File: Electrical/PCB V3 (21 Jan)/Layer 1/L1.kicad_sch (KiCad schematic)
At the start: 219 parts, among them J1 Conn_01x04, J2 Conn_01x02, Q1 NMOS, U1 LM2587S-ADJ, U2 CD74HC4067SM, U3 CD74HC4067SM, U4 XT30UPB-M, U5 113991054

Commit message: added some stuff to parts list, fixed l1 schematics to fit parts in lab abit more, pending change of activaition circuit
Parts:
- removed L1, L10, L11, L12, L13, L14, L15, L16, L17, L18, L19, L2, L20, L21, L22, L23, L24, L25, L26, L27, L28, L29, L3, L30, L31, L32, L4, L5, L6, L7, L8, L9: 10µH, Inductor_SMD:L_0805_2012Metric, symbol pspice:INDUCTOR
- added Q3: NMOS, Package_TO_SOT_THT:TO-220-3_Vertical, symbol Simulation_SPICE:NMOS
- R35: value 36.9K -> 36.9K/56k
- R36: value 2K -> 2K/2.94k
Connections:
- net GND: now also Q3.3 (S)
- net Solenoid Activation: now also Q3.2 (G); no longer Q1.2 (G)
- net at LED6.2 (A): now also R6.2
- net at LED32.2 (A): now also R32.2
- net at LED5.2 (A): now also R5.2
- net at LED18.2 (A): now also R18.2
- net at LED4.2 (A): now also R4.2
- net at LED8.2 (A): now also R8.2
- net at R9.2: now also LED9.2 (A)
- net at LED30.2 (A): now also R30.2
- net at LED31.2 (A): now also R31.2
- net at R28.2: now also LED28.2 (A)
- net at R29.2: now also LED29.2 (A)
- net at LED26.2 (A): now also R26.2
- net at LED17.2 (A): now also R17.2
- net at LED19.2 (A): now also R19.2
- net at R21.2: now also LED21.2 (A)
- net at LED7.2 (A): now also R7.2
- net at LED10.2 (A): now also R10.2
- net at LED14.2 (A): now also R14.2
- net at LED3.2 (A): now also R3.2
- net at LED25.2 (A): now also R25.2
- net at LED2.2 (A): now also R2.2
- net at LED16.2 (A): now also R16.2
- net at LED20.2 (A): now also R20.2
- net at LED1.2 (A): now also R1.2
- net at LED24.2 (A): now also R24.2
- net at LED27.2 (A): now also R27.2
- net at R13.2: now also LED13.2 (A)
- net at LED12.2 (A): now also R12.2
- net at R15.2: now also LED15.2 (A)
- net at LED11.2 (A): now also R11.2
- net at LED23.2 (A): now also R23.2
- net at R22.2: now also LED22.2 (A)
- new net: Q1.2 (G), Q3.1 (D)
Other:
- moved on the sheet: D2, LED1, LED10, LED11, LED12, LED13, LED14, LED15, LED16, LED17, LED18, LED19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

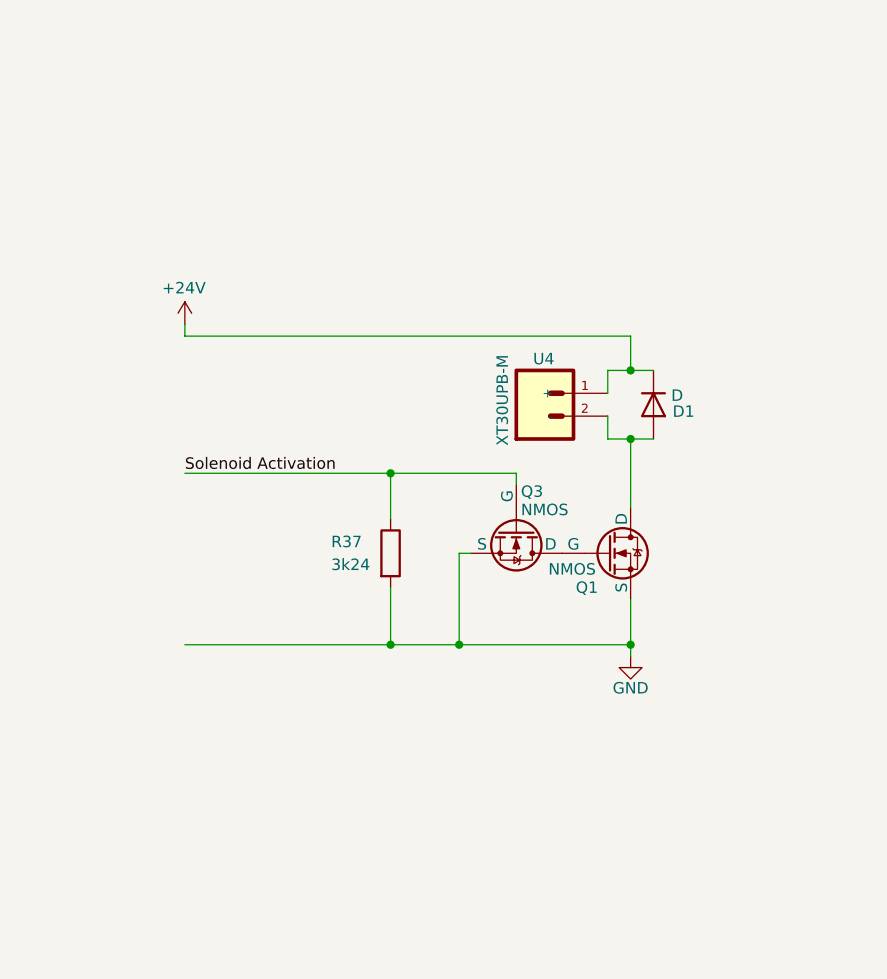
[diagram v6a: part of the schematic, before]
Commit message: fixed l1 solenoid activation circuit
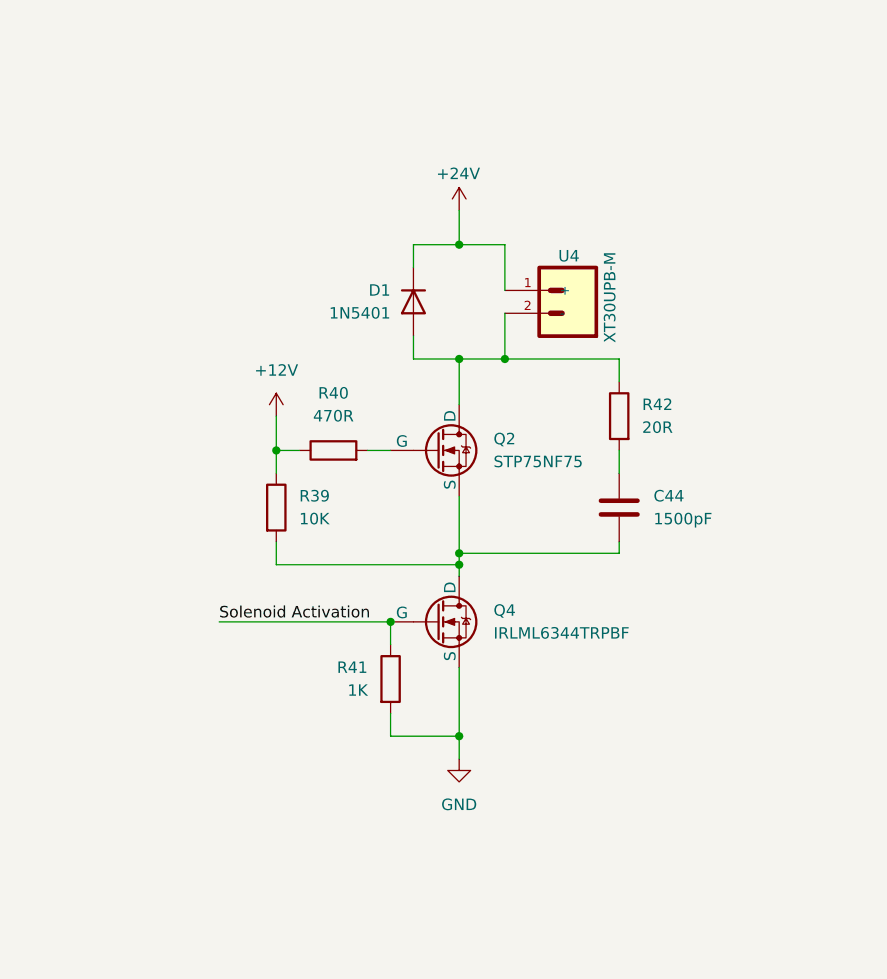
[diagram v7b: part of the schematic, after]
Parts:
- removed D1: D, Diode_THT:D_DO-201AD_P15.24mm_Horizontal, symbol Device:D
- removed Q1, Q3: NMOS, Package_TO_SOT_THT:TO-220-3_Vertical, symbol Simulation_SPICE:NMOS
- removed R37: 3k24, Capacitor_SMD:C_0603_1608Metric, symbol Device:R
- added C44: 1500pF, Capacitor_SMD:C_0603_1608Metric, symbol Device:C
- added D1: 1N5401, Diode_THT:D_DO-201AD_P15.24mm_Horizontal, symbol Diode:1N5401
- added Q2: STP75NF75, stolen_activation_moosfits:TO-220-3_Vertical, symbol vincent:IPD050N10N5ATMA1
- added Q4: IRLML6344TRPBF, stolen_activation_moosfits:SOT95P237X112-3N, symbol vincent:IRLML6344TRPBF
- added R39: 10K, Resistor_SMD:R_0603_1608Metric, symbol Device:R
- added R40: 470R, Resistor_SMD:R_0603_1608Metric, symbol Device:R
- added R41: 1K, Resistor_SMD:R_0603_1608Metric, symbol Device:R
- added R42: 20R, Resistor_SMD:R_0603_1608Metric, symbol Device:R
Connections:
- net +12V: now also R39.1, R40.1
- net +24V: now also D1.1 (K)
- net GND: now also Q4.2 (S), R41.2
- net Solenoid Activation: now also Q4.1 (G), R41.1
- net at U4.2 (-): now also D1.2 (A), Q2.2 (D), R42.1
- new net: C44.2, Q2.3 (S), Q4.3 (D), R39.2
- new net: Q2.1 (G), R40.2
- new net: C44.1, R42.2
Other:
- moved on the sheet: U4
